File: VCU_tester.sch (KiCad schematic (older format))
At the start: 40 parts, among them J1 Conn_01x04_Male, J12 Conn_01x08_Male, J13 Conn_01x08_Male, J14 USB_C_Receptacle, J15 USB_B_Micro, J2 Screw_Terminal_01x02, J500 Conn_01x10_Female, J501 Conn_01x08_Female, J502 Conn_01x08_Female, J503 Conn_01x08_Female, J504 Conn_01x08_Female, J505 Conn_01x08_Female, J507 Conn_02x18_Odd_Even, J7 Conn_01x04_Male, P8 BeagleBone_Black_Header, P9 BeagleBone_Black_Header, U1 REF3020, U6 DS3231MZ, U7 DS3231MZ

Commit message: fix sch vcu connections
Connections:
- net +5V: no longer J501.5 (Pin_5), J501.8 (Pin_8), J507.1 (Pin_1), J507.2 (Pin_2), TP3.1
- net GPIO_45: no longer J507.4 (Pin_4)
- net GPIO_46: no longer J507.5 (Pin_5)
- net GPIO_50: no longer J507.9 (Pin_9)
- net PD27: no longer J505.2 (Pin_2)
- net PD28: no longer J505.1 (Pin_1)
- net PressLin: now also J507.5 (Pin_5); no longer J507.31 (Pin_31)
- net PressLout: now also J507.4 (Pin_4); no longer J507.34 (Pin_34)
- net AIR1: no longer names the net of J507.32 (Pin_32)
- net AIR2: no longer names the net of J507.30 (Pin_30)
- net AIR3: no longer names the net of J507.29 (Pin_29)
- net VCUCANRX1: no longer names the net of J507.33 (Pin_33)
- net VCUGPIO_10 renamed VCUTXD2A
- net VCUGPIO_11: no longer names the net of J500.4 (Pin_4)
- net VCUGPIO_12: no longer names the net of J500.5 (Pin_5)
- net VCUGPIO_4: no longer names the net of J503.5 (Pin_5)
- net VCUGPIO_5: no longer names the net of J503.6 (Pin_6)
- net VCUGPIO_8: no longer names the net of J500.1 (Pin_1)
- net VCUTXD1: no longer names the net of J507.28 (Pin_28)
- new net +5VA: J501.5 (Pin_5), J501.8 (Pin_8), J507.1 (Pin_1), J507.2 (Pin_2), TP3.1
- new net TWCK2: J505.1 (Pin_1)
- new net TWD2: J505.2 (Pin_2)
- no-connect marks 116 -> 122
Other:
- note added: "ADVREF"
- note added: "Changes made:\nPD25 (J500-3) fixed to VCUTXD2A\nPressLin,PressLout moved to correct pins\nJ507-10 corrected to NC, please remove GPIO_51 connection\nRemoved:\n J507-4 to GPIO_45\n J507-5 to GPIO_46\n J507-9 (PA5, uart) to GPIO_50"
- note added: "GND"
- note added: "PA1"
- note added: "PA10"
- note added: "PA12"
- note added: "PA13"
- note added: "PA17"
- note added: "PA18"
- note added: "PA19"
- note added: "PA2"
- note added: "PA21"
- note added: "PA22"
- note added: "PA23"
- note added: "PA24"
- note added: "PA25"
- note added: "PA26"
- note added: "PA28"
- note added: "PA29"
- note added: "PA3"
- note added: "PA30"
- note added: "PA31"
- note added: "PA4"
- note added: "PA5"
- note added: "PA6"
- note added: "PB0"
- note added: "PB1"
- note added: "PB13"
- note added: "PB2"
- note added: "PB3"
- note added: "PB4"
- note added: "PC12"
- note added: "PC13"
- note added: "PC14"
- note added: "PC19"
- note added: "PC30"
- note added: "PC31"
- note added: "PC9"
- note added: "PD0"
- note added: "PD11"
- note added: "PD15"
- note added: "PD16"
- note added: "PD17"
- note added: "PD18"
- note added: "PD19"
- note added: "PD20"
- note added: "PD21"
- note added: "PD22"
- note added: "PD24"
- note added: "PD25"
- note added: "PD26"
- note added: "PD27"
- note added: "PD28"
- note added: "PD30"
- note added: "Recommended changes:\nRemove J507-27 to GPIO_22\nReview gpio assignments\nUSB-C CC1/2 each needs 5.1k pulldown"
- note removed: "tsal state"
- moved on the sheet: J14, J15, J502, J503, J504, J505, TP1, TP2, TP3, U1

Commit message: fix sch beaglebone connections
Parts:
- P8, P9: Part 1528-1365-ND -> (none)
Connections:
- net PD27 is gone; now on net TWD2: R10.2, U7.7 (SDA)
- net PD28 is gone; now on net TWCK2: R8.2, U7.8 (SCL)
- net GPIO_4: no longer P9.18 (Pin_18), R7.2, U6.8 (SCL)
- net GPIO_5: no longer P9.17 (Pin_17), R9.2, U6.7 (SDA)
- net GPIO_51: no longer J507.10 (Pin_10)
- net VCURXD2A: now also J500.3 (Pin_3)
- net VCUTXD2A: no longer J500.3 (Pin_3)
- net GPIO_32 renamed MMC1_DAT0
- net GPIO_33 renamed MMC1_DAT1
- net GPIO_36 renamed MMC1_DAT4
- net GPIO_37 renamed MMC1_DAT5
- net GPIO_62 renamed MMC1_CLK
- net GPIO_63 renamed MMC1_CMD
- net MMC1_Dat2 renamed MMC1_DAT2
- net MMC1_Dat6 renamed MMC1_DAT6
- net MMC1_dat3 renamed MMC1_DAT3
- net MMC1_dat7 renamed MMC1_DAT7
- new net I2C1_SCL: P9.17 (Pin_17), R7.2, U6.8 (SCL)
- new net I2C1_SDA: P9.18 (Pin_18), R9.2, U6.7 (SDA)
- no-connect marks 122 -> 124
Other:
- note added: "Can we have usb power ports and bb ethernet facing the same edge?"
- note added: "Changes made:\nPD25 (J500-3) fixed to VCURXD2A\nPressLin,PressLout moved to correct pins\nJ507-10 corrected to NC\nConnection to RTC Beagle fixed: SCL/SDA swapped\nRemoved:\n J507-4 (adc) to GPIO_45\n J507-5 (adc) to GPIO_46\n J507-9 (uart) to GPIO_50\n J507-10 (nc) to GPIO_51"
- note added: "GPIO_4"
- note added: "GPIO_5"
- note added: "Recommended changes:\nRemove J507-27 to GPIO_22\nReview gpio assignments\nUSB-C CC1/2 each needs 5.1k pulldown\nUse keystone 1060 cr2032 holder, it looks less jank"
- note added: "wtf is up with VCU{TX,RX}D2 and VCU{TX,RX}D2A ???"
- note removed: "Changes made:\nPD25 (J500-3) fixed to VCUTXD2A\nPressLin,PressLout moved to correct pins\nJ507-10 corrected to NC, please remove GPIO_51 connection\nRemoved:\n J507-4 to GPIO_45\n J507-5 to GPIO_46\n J507-9 (PA5, uart) to GPIO_50"
- note removed: "Recommended changes:\nRemove J507-27 to GPIO_22\nReview gpio assignments\nUSB-C CC1/2 each needs 5.1k pulldown"
- moved on the sheet: BT1, D1, J1, J2, J7, R10, R3, R4, R5, R7, R8, R9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

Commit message: Lots of layout, power bus
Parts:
- removed TP44: TestPoint, Connector_PinHeader_2.54mm:PinHeader_1x01_P2.54mm_Vertical, symbol Connector:TestPoint
- added TP5, TP6, TP7, TP8: TestPoint, Connector_PinHeader_2.54mm:PinHeader_1x01_P2.54mm_Vertical, symbol Connector:TestPoint
- BT1: footprint Battery:BatteryHolder_MPD_BC2003_1x2032 -> Battery:BatteryHolder_Keystone_1060_1x2032
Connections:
- net +5VA is gone; now on net +5V: J501.5 (Pin_5), J501.8 (Pin_8), J507.1 (Pin_1), J507.2 (Pin_2), TP3.1
- net +3V3: now also TP8.1
- net +5V: now also TP7.1
- net GNDD: now also TP5.1, TP6.1
- net GPIO_22: no longer J507.27 (Pin_27)
- no-connect marks 124 -> 125
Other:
- note added: "Changes made (Andrew):\nPD25 (J500-3) fixed to VCURXD2A\nPressLin,PressLout moved to correct pins\nJ507-10 corrected to NC\nConnection to RTC Beagle fixed: SCL/SDA swapped\nRemoved:\n J507-4 (adc) to GPIO_45\n J507-5 (adc) to GPIO_46\n J507-9 (uart) to GPIO_50\n J507-10 (nc) to GPIO_51"
- note added: "Changes made (Will):\nBoard initial layout done (NEED GPIOs)\nChanged power bus\n"
- note added: "TODO:\n0) Assign new GPIOs on VCU\n1) ADD RES TO CP1/2 ON USBC\n2) ADD SILKSCREEN FOR WHAT TESTPOINTS ARE!!! (GPIO out of VCU??)\n3) CHANGE FOOTPRINT OF TCAN"
- note removed: "Can we have usb power ports and bb ethernet facing the same edge?"
- note removed: "Changes made:\nPD25 (J500-3) fixed to VCURXD2A\nPressLin,PressLout moved to correct pins\nJ507-10 corrected to NC\nConnection to RTC Beagle fixed: SCL/SDA swapped\nRemoved:\n J507-4 (adc) to GPIO_45\n J507-5 (adc) to GPIO_46\n J507-9 (uart) to GPIO_50\n J507-10 (nc) to GPIO_51"
- moved on the sheet: J12, TP43, TP45, TP46, TP47, TP48

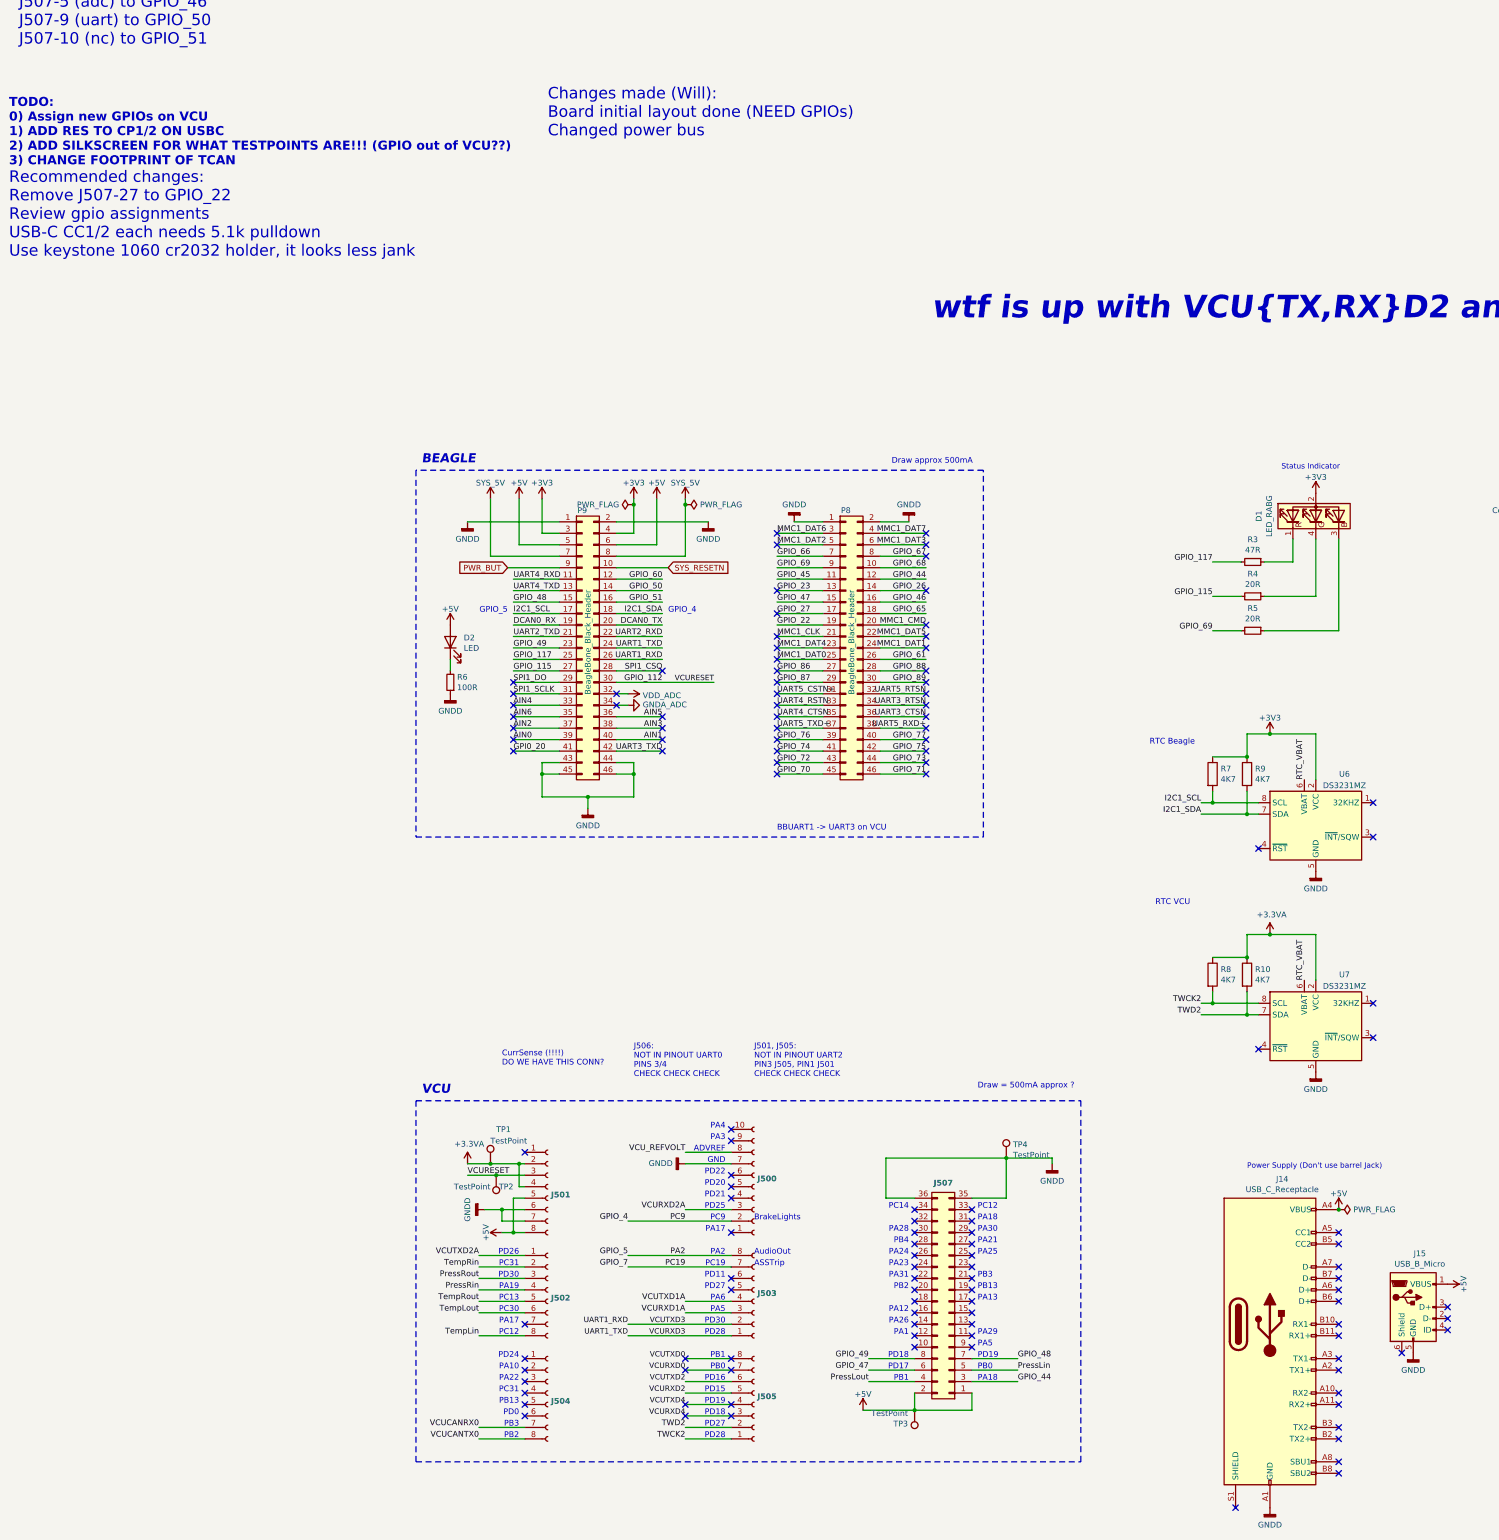
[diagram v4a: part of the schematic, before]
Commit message: decouple caps, moved testpoint for usb access, tcan footprints
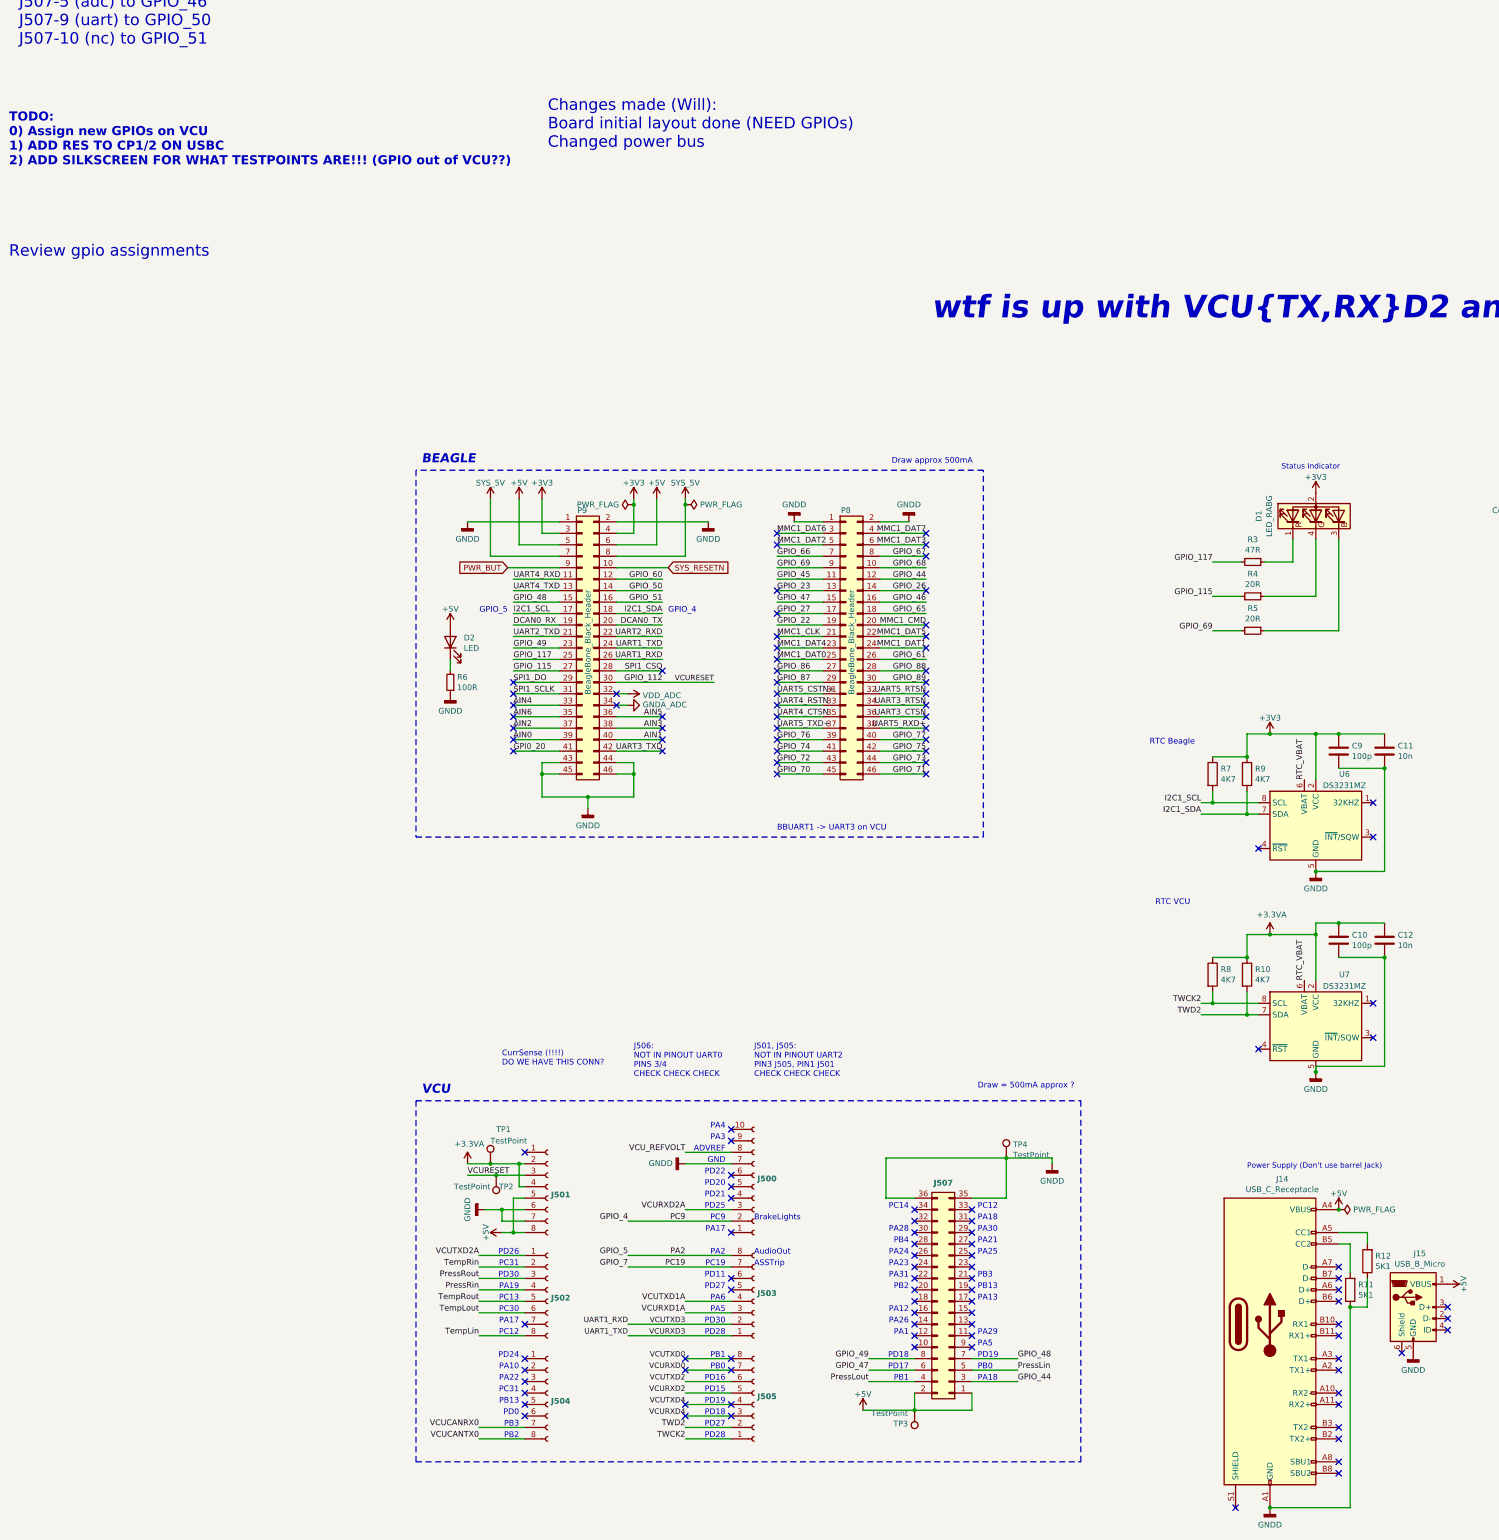
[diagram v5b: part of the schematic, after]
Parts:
- added C10, C9: 100p, Capacitor_SMD:C_0805_2012Metric_Pad1.15x1.40mm_HandSolder, symbol Device:C
- added C11, C12: 10n, Capacitor_SMD:C_0805_2012Metric_Pad1.15x1.40mm_HandSolder, symbol Device:C
- added R11, R12: 5K1, Resistor_SMD:R_0805_2012Metric_Pad1.15x1.40mm_HandSolder, symbol Device:R
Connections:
- net +3.3VA: now also C10.1, C12.1
- net +3V3: now also C11.1, C9.1
- net GNDD: now also C10.2, C11.2, C12.2, C9.2, R11.1, R12.1
- net at J14.A5 (CC1): now also R12.2
- net at J14.B5 (CC2): now also R11.2
- no-connect marks 125 -> 123
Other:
- note added: "TODO:\n0) Assign new GPIOs on VCU\n1) ADD RES TO CP1/2 ON USBC\n2) ADD SILKSCREEN FOR WHAT TESTPOINTS ARE!!! (GPIO out of VCU??)"
- note added: "\nReview gpio assignments\n"
- note removed: "Recommended changes:\nRemove J507-27 to GPIO_22\nReview gpio assignments\nUSB-C CC1/2 each needs 5.1k pulldown\nUse keystone 1060 cr2032 holder, it looks less jank"
- note removed: "TODO:\n0) Assign new GPIOs on VCU\n1) ADD RES TO CP1/2 ON USBC\n2) ADD SILKSCREEN FOR WHAT TESTPOINTS ARE!!! (GPIO out of VCU??)\n3) CHANGE FOOTPRINT OF TCAN"
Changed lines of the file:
@@
 NoConn ~ 9000 9650
 NoConn ~ 9000 9550
-NoConn ~ 9000 7650
-NoConn ~ 9000 7550
 $Comp
 L power:GNDD #PWR0103
@@
 	8200 3200 8400 3200
 Connection ~ 8200 3400
-Wire Wire Line
-	8400 3200 8800 3200
-Wire Wire Line
-	8800 3200 8800 3600
 Connection ~ 8400 3200
 NoConn ~ 9300 4100
@@
 NoConn ~ 5800 7450
 Text Notes -2600 -950 0    100  ~ 0
-Recommended changes:\nRemove J507-27 to GPIO_22\nReview gpio assignments\nUSB-C CC1/2 each needs 5.1k pulldown\nUse keystone 1060 cr2032 holder, it looks less jank
+\nReview gpio assignments\n
 NoConn ~ 5300 8550
 Text Notes 5850 8550 0    50   ~ 0
@@
 $EndComp
 Text Notes -2600 -1750 0    79   ~ 16
-TODO:\n0) Assign new GPIOs on VCU\n1) ADD RES TO CP1/2 ON USBC\n2) ADD SILKSCREEN FOR WHAT TESTPOINTS ARE!!! (GPIO out of VCU??)\n3) CHANGE FOOTPRINT OF TCAN
-Text Notes 2100 -2000 0    100  ~ 0
+TODO:\n0) Assign new GPIOs on VCU\n1) ADD RES TO CP1/2 ON USBC\n2) ADD SILKSCREEN FOR WHAT TESTPOINTS ARE!!! (GPIO out of VCU??)
+Text Notes 2100 -1900 0    100  ~ 0
 Changes made (Will):\nBoard initial layout done (NEED GPIOs)\nChanged power bus\n
+$Comp
+L Device:C C10
+U 1 1 5F03FB02
+P 9000 5000
+F 0 "C10" H 9115 5046 50  0000 L CNN
+F 1 "100p" H 9115 4955 50  0000 L CNN
+F 2 "Capacitor_SMD:C_0805_2012Metric_Pad1.15x1.40mm_HandSolder" H 9038 4850 50  0001 C CNN
+F 3 "~" H 9000 5000 50  0001 C CNN
+	1    9000 5000
+	1    0    0    -1
+$EndComp
+$Comp
+L Device:C C12
+U 1 1 5F0588C3
+P 9400 5000
+F 0 "C12" H 9515 5046 50  0000 L CNN
+F 1 "10n" H 9515 4955 50  0000 L CNN
+F 2 "Capacitor_SMD:C_0805_2012Metric_Pad1.15x1.40mm_HandSolder" H 9438 4850 50  0001 C CNN
+F 3 "~" H 9400 5000 50  0001 C CNN
+	1    9400 5000
+	1    0    0    -1
+$EndComp
+Wire Wire Line
+	8800 4950 8800 4850
+Wire Wire Line
+	8800 4850 9000 4850
+Connection ~ 8800 4950
+Connection ~ 9000 4850
+Wire Wire Line
+	9000 4850 9400 4850
+Wire Wire Line
+	9000 5150 9400 5150
+Wire Wire Line
+	9400 5150 9400 6100
+Wire Wire Line
+	9400 6100 8800 6100
+Wire Wire Line
+	8800 6100 8800 6150
+Connection ~ 9400 5150
+Connection ~ 8800 6150
+$Comp
+L Device:C C9
+U 1 1 5F0BE09F
+P 9000 3350
+F 0 "C9" H 9115 3396 50  0000 L CNN
+F 1 "100p" H 9115 3305 50  0000 L CNN
+F 2 "Capacitor_SMD:C_0805_2012Metric_Pad1.15x1.40mm_HandSolder" H 9038 3200 50  0001 C CNN
+F 3 "~" H 9000 3350 50  0001 C CNN
+	1    9000 3350
+	1    0    0    -1
+$EndComp
+$Comp
+L Device:C C11
+U 1 1 5F0BE0A5
+P 9400 3350
+F 0 "C11" H 9515 3396 50  0000 L CNN
+F 1 "10n" H 9515 3305 50  0000 L CNN
+F 2 "Capacitor_SMD:C_0805_2012Metric_Pad1.15x1.40mm_HandSolder" H 9438 3200 50  0001 C CNN
+F 3 "~" H 9400 3350 50  0001 C CNN
+	1    9400 3350
+	1    0    0    -1
+$EndComp
+Connection ~ 9000 3200
+Wire Wire Line
+	9000 3200 9400 3200
+Wire Wire Line
+	9000 3500 9400 3500
+Wire Wire Line
+	9400 3500 9400 4400
+Connection ~ 9400 3500
+Wire Wire Line
+	8800 4400 9400 4400
+Connection ~ 8800 4400
+Wire Wire Line
+	8400 3200 8800 3200
+Wire Wire Line
+	8800 3200 8800 3600
+Connection ~ 8800 3200
+Wire Wire Line
+	8800 3200 9000 3200
+$Comp
+L Device:R R11
+U 1 1 5F164F59
+P 9100 8050
+F 0 "R11" H 9030 8004 50  0000 R CNN
+F 1 "5K1" H 9030 8095 50  0000 R CNN
+F 2 "Resistor_SMD:R_0805_2012Metric_Pad1.15x1.40mm_HandSolder" V 9030 8050 50  0001 C CNN
+F 3 "~" H 9100 8050 50  0001 C CNN
+	1    9100 8050
+	-1   0    0    1
+$EndComp
+$Comp
+L Device:R R12
+U 1 1 5F186EC3
+P 9250 7800
+F 0 "R12" H 9180 7754 50  0000 R CNN
+F 1 "5K1" H 9180 7845 50  0000 R CNN
+F 2 "Resistor_SMD:R_0805_2012Metric_Pad1.15x1.40mm_HandSolder" V 9180 7800 50  0001 C CNN
+F 3 "~" H 9250 7800 50  0001 C CNN
+	1    9250 7800
+	-1   0    0    1
+$EndComp
+Wire Wire Line
+	9100 7900 9100 7650
+Wire Wire Line
+	9100 7650 9000 7650
+Wire Wire Line
+	9000 7550 9250 7550
+Wire Wire Line
+	9250 7550 9250 7650
+Wire Wire Line
+	9250 7950 9250 8200
+Wire Wire Line
+	9250 8200 9100 8200
+Wire Wire Line
+	8400 9950 9100 9950
+Wire Wire Line
+	9100 9950 9100 8200
+Connection ~ 8400 9950
+Connection ~ 9100 8200
 $EndSCHEMATC
